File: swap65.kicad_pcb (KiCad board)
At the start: 2 copper layers, 309.6 x 100 mm, 167 parts, among them J1 SWD, J2 USB_C_Receptacle_USB2.0, SW1 SW_Push, SW10 Z, SW11 LWin, SW12 2, SW13 W, SW14 S, SW15 X, SW16 LAlt, SW17 3, SW18 E, SW19 D, SW2 Esc, SW20 C, SW21 4, SW22 R, SW23 F, SW24 V, SW25 5, SW26 T, SW27 G, SW28 B, SW29 Space, SW3 Tab, SW30 6, SW31 Y, SW32 H, SW33 N, SW34 7, SW35 U, SW36 J, SW37 M, SW38 8, SW39 I, SW4 Caps, SW40 K, SW41 Comma, SW42 9, SW43 O, SW44 L, SW45 Period, SW46 RAlt, SW47 0, SW48 P, SW49 Colon, SW5 LShift, SW50 Slash, SW51 Fn, SW52 Minus, SW53 [, SW54 Quote, SW55 Plus, SW56 ], SW57 Enter, SW58 RShift, SW59 Left, SW6 LCtrl, SW60 Pipe, SW61 BkSlsh, SW62 Up, SW63 Down, SW64 BkSpc, SW65 Tilde, SW66 Right, SW7 1, SW8 Q, SW9 A, U1 RP2040, U2 USBLC6-2SC6, U3 XC6206PxxxMR, U4 W25Q128JVS, Y1 12MHz

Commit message: routed columns
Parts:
- removed the J1 at (346.4, 143.6)
- added SW2: SW_Push, Button_Switch_SMD:SW_SPST_SKQG_WithStem, B.Cu at (351.3, 142.3)
- moved R3 8.39 mm to (347.0, 132.5), turned to 0 degrees
- moved C9 0.17 mm to (357.7, 128.8)
- turned S2 to 0 degrees
- renumbered C3 to C2, C4 to C3, C2 to C4, D57 to D56, D58 to D57, D59 to D58, D60 to D59, D56 to D60, J2 to J1, SW9 to SW10, SW10 to SW11, SW11 to SW12, SW12 to SW13, SW13 to SW14, SW14 to SW15, SW15 to SW16, SW16 to SW17, SW17 to SW18, SW18 to SW19, SW19 to SW20, SW20 to SW21, SW21 to SW22, SW22 to SW23, SW23 to SW24, SW24 to SW25, SW25 to SW26, SW26 to SW27, SW27 to SW28, SW28 to SW29, SW2 to SW3, SW29 to SW30, SW30 to SW31, SW31 to SW32, SW32 to SW33, SW33 to SW34, SW34 to SW35, SW35 to SW36, SW36 to SW37, SW37 to SW38, SW38 to SW39, SW3 to SW4, SW39 to SW40, SW40 to SW41, SW41 to SW42, SW42 to SW43, SW43 to SW44, SW44 to SW45, SW45 to SW46, SW46 to SW47, SW47 to SW48, SW48 to SW49, SW4 to SW5, SW49 to SW50, SW50 to SW51, SW51 to SW52, SW52 to SW53, SW53 to SW54, SW54 to SW55, SW55 to SW56, SW56 to SW57, SW5 to SW6, SW57 to SW62, SW62 to SW63, SW63 to SW64, SW64 to SW65, SW65 to SW66, SW66 to SW67, SW6 to SW7, SW7 to SW8, SW8 to SW9
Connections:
- net Net-(C3-Pad2) renamed /XIN
- net Net-(C4-Pad2) renamed /XOUT
- D1 pad 1: ROW1 -> ROW0
- D10 pad 1: ROW5 -> ROW4
- D11 pad 1: ROW1 -> ROW0
- D12 pad 1: ROW2 -> ROW1
- D13 pad 1: ROW3 -> ROW2
- D14 pad 1: ROW4 -> ROW3
- D15 pad 1: ROW5 -> ROW4
- D16 pad 1: ROW1 -> ROW0
- D17 pad 1: ROW2 -> ROW1
- D18 pad 1: ROW3 -> ROW2
- D19 pad 1: ROW4 -> ROW3
- D2 pad 1: ROW2 -> ROW1
- D20 pad 1: ROW1 -> ROW0
- D21 pad 1: ROW2 -> ROW1
- D22 pad 1: ROW3 -> ROW2
- D23 pad 1: ROW4 -> ROW3
- D24 pad 1: ROW1 -> ROW0
- D25 pad 1: ROW2 -> ROW1
- D26 pad 1: ROW3 -> ROW2
- D27 pad 1: ROW4 -> ROW3
- D28 pad 1: ROW5 -> ROW4
- D29 pad 1: ROW1 -> ROW0
- D3 pad 1: ROW3 -> ROW2
- D30 pad 1: ROW2 -> ROW1
- D31 pad 1: ROW3 -> ROW2
- D32 pad 1: ROW4 -> ROW3
- D33 pad 1: ROW1 -> ROW0
- D34 pad 1: ROW2 -> ROW1
- D35 pad 1: ROW3 -> ROW2
- D36 pad 1: ROW4 -> ROW3
- D37 pad 1: ROW1 -> ROW0
- D38 pad 1: ROW2 -> ROW1
- D39 pad 1: ROW3 -> ROW2
- D4 pad 1: ROW4 -> ROW3
- D40 pad 1: ROW4 -> ROW3
- D41 pad 1: ROW1 -> ROW0
- D42 pad 1: ROW2 -> ROW1
- D43 pad 1: ROW3 -> ROW2
- D44 pad 1: ROW4 -> ROW3
- D45 pad 1: ROW5 -> ROW4
- D46 pad 1: ROW1 -> ROW0
- D47 pad 1: ROW2 -> ROW1
- D48 pad 1: ROW3 -> ROW2
- D49 pad 1: ROW4 -> ROW3
- D5 pad 1: ROW5 -> ROW4
- D50 pad 1: ROW5 -> ROW4
- D51 pad 1: ROW1 -> ROW0
- D52 pad 1: ROW2 -> ROW1
- D53 pad 1: ROW3 -> ROW2
- D54 pad 1: ROW1 -> ROW0
- D55 pad 1: ROW2 -> ROW1
- D56 pad 1: ROW4 -> ROW3
- D57 pad 1: ROW5 -> ROW4
- D58 pad 1: ROW1 -> ROW0
- D59 pad 1: ROW2 -> ROW1
- D6 pad 1: ROW1 -> ROW0
- D60 pad 1: ROW3 -> ROW2
- D61 pad 1: ROW4 -> ROW3
- D62 pad 1: ROW5 -> ROW4
- D63 pad 1: ROW1 -> ROW0
- D64 pad 1: ROW5 -> ROW4
- D7 pad 1: ROW2 -> ROW1
- D8 pad 1: ROW3 -> ROW2
- D9 pad 1: ROW4 -> ROW3
- U1 pad 11: unconnected-(U1-Pad11) -> COL6
- U1 pad 12: unconnected-(U1-Pad12) -> COL5
- U1 pad 13: unconnected-(U1-Pad13) -> COL4
- U1 pad 14: unconnected-(U1-Pad14) -> COL3
- U1 pad 15: unconnected-(U1-Pad15) -> COL2
- U1 pad 16: unconnected-(U1-Pad16) -> COL1
- U1 pad 17: unconnected-(U1-Pad17) -> COL0
- U1 pad 2: unconnected-(U1-Pad2) -> COL14
- U1 pad 24: SWCLK -> unconnected-(U1-Pad24)
- U1 pad 25: SWD -> unconnected-(U1-Pad25)
- U1 pad 3: unconnected-(U1-Pad3) -> COL13
- U1 pad 4: unconnected-(U1-Pad4) -> COL12
- U1 pad 5: unconnected-(U1-Pad5) -> COL11
- U1 pad 6: unconnected-(U1-Pad6) -> COL10
- U1 pad 7: unconnected-(U1-Pad7) -> COL9
- U1 pad 8: unconnected-(U1-Pad8) -> COL8
- U1 pad 9: unconnected-(U1-Pad9) -> COL7
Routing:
- net COL0: track 85.1 -> 392.7 mm, vias 0 -> 1
- net ROW5: track 283.9 -> 0.00 mm
- net COL1: track 96.3 -> 376.3 mm, vias 0 -> 1
- net COL2: track 91.0 -> 352.2 mm, vias 0 -> 1
- net ROW0: track 0.00 -> 255.1 mm
- net COL3: track 67.0 -> 306.8 mm, vias 0 -> 1
- net COL4: track 67.0 -> 288.2 mm, vias 0 -> 1
- net COL5: track 87.0 -> 290.2 mm, vias 0 -> 1
- net COL6: track 67.0 -> 251.8 mm, vias 0 -> 1
- net COL7: track 67.0 -> 251.3 mm, vias 0 -> 1
- net COL8: track 67.0 -> 234.9 mm, vias 0 -> 1
- net COL9: track 87.0 -> 229.0 mm, vias 0 -> 1
- net COL11: track 44.0 -> 182.6 mm, vias 0 -> 1
- net COL10: track 87.0 -> 210.9 mm, vias 0 -> 1
- net COL12: track 84.1 -> 183.9 mm, vias 0 -> 1
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
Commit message: completed first pass at routing
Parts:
- SW60, SW65, SW66: footprint marbastlib-mx:SW_MX_HS_1u -> marbastlib-mx:SW_MX_HS_S_1u
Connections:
- U1 pad 29: unconnected-(U1-Pad29) -> ROW4
- U1 pad 30: unconnected-(U1-Pad30) -> ROW3
- U1 pad 31: unconnected-(U1-Pad31) -> ROW2
- U1 pad 35: unconnected-(U1-Pad35) -> ROW1
- U1 pad 36: unconnected-(U1-Pad36) -> ROW0
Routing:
- net ROW4: track 286.4 -> 333.7 mm, vias 0 -> 2
- net ROW3: track 254.8 -> 297.8 mm, vias 0 -> 2
- net ROW0: track 255.1 -> 293.7 mm
- net ROW2: track 247.7 -> 283.6 mm
- net ROW1: track 257.2 -> 271.1 mm
- net Net-(D58-Pad2): track 28.6 -> 27.0 mm
- net COL0: track 392.7 -> 391.2 mm

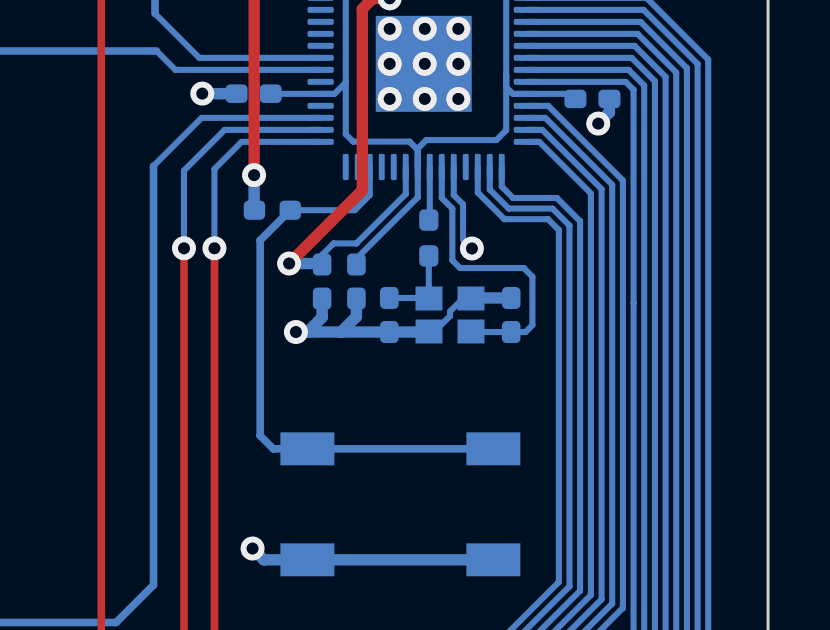
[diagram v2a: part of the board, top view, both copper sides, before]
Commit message: added screen header to schematic
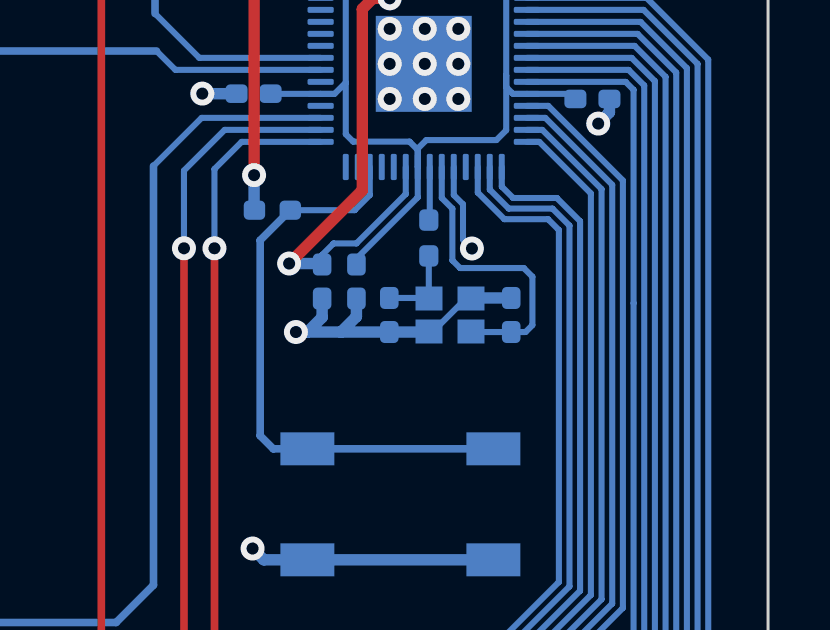
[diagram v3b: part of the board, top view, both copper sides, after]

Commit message: completed route pass 1
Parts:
- added J2: OLED, Connector_PinHeader_2.54mm:PinHeader_1x04_P2.54mm_Vertical, F.Cu at (350.5, 154.9)
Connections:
- U1 pad 38: unconnected-(U1-Pad38) -> SCL
- U1 pad 39: unconnected-(U1-Pad39) -> SDA

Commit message: routed usb and jst connector
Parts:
- removed the R5 at (346.2, 99.4)
- added J3: DB, Connector_JST:JST_SH_SM04B-SRSS-TB_1x04-1MP_P1.00mm_Horizontal, B.Cu at (352.7, 117.9)
- U2: value USBLC6-2SC6 -> SRV05-4; footprint Package_TO_SOT_SMD:SOT-23-6 -> marbastlib-various:SOT-23-6-routable
- moved J2 36.2 mm to (345.2, 119.1)
- moved C1 21.4 mm to (365.8, 120.7), turned to 180 degrees
- moved C10 19.3 mm to (348.2, 138.7), turned to 180 degrees
- moved C16 18.7 mm to (359.9, 136.2), turned to 0 degrees
- moved C11 17.3 mm to (358.1, 130.8), turned to 0 degrees
- moved R3 16.6 mm to (352.9, 148.1), turned to -90 degrees
- moved C15 16.3 mm to (355.9, 140.7), turned to -90 degrees
- moved R1 12.9 mm to (357.6, 128.8)
- moved R2 12.9 mm to (356.1, 128.8)
- moved SW1 11.9 mm to (371.0, 104.3)
- moved R5 11.9 mm to (367.0, 108.0)
- moved C6 11.7 mm to (358.1, 131.9)
- moved SW2 11.6 mm to (351.0, 153.9), turned to -90 degrees
- moved C2 10.2 mm to (349.1, 144.3), turned to 180 degrees
- moved U3 10.1 mm to (368.3, 115.2)
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- renumbered C17 to C1, C7 to C10, C8 to C11, C9 to C12, C10 to C13, C11 to C14, C12 to C15, C13 to C16, C14 to C17, C15 to C4, C16 to C5, C1 to C6, C4 to C7, C5 to C8, C6 to C9, R8 to R5, U4 to U3, U3 to U4
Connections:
- J1 pad A6: D_USB_P -> D_P
- J1 pad A7: D_USB_N -> D_N
- J1 pad B6: D_USB_P -> D_P
- J1 pad B7: D_USB_N -> D_N
- J1 pad S1: Net-(J1-PadS1) -> GND
- U2 pad 1: D_P -> unconnected-(U2-Pad1)
- U2 pad 3: D_N -> D_P
- U2 pad 4: D_USB_N -> D_N
- U2 pad 5: +5V -> VBUS
- U2 pad 6: D_USB_P -> unconnected-(U2-Pad6)
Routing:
- net COL0: track 391.2 -> 0.00 mm, vias 1 -> 0
- net COL1: track 376.3 -> 0.00 mm, vias 1 -> 0
- net COL2: track 352.2 -> 0.00 mm, vias 1 -> 0
- net ROW4: track 333.7 -> 0.00 mm, vias 2 -> 0
- net COL3: track 306.8 -> 0.00 mm, vias 1 -> 0
- net ROW3: track 297.8 -> 0.00 mm, vias 2 -> 0
- net ROW0: track 293.7 -> 0.00 mm
- net COL5: track 290.2 -> 0.00 mm, vias 1 -> 0
- net COL4: track 288.2 -> 0.00 mm, vias 1 -> 0
- net ROW2: track 283.6 -> 0.00 mm
- net ROW1: track 271.1 -> 0.00 mm
- net COL6: track 251.8 -> 0.00 mm, vias 1 -> 0
- net COL7: track 251.3 -> 0.00 mm, vias 1 -> 0
- net COL8: track 234.9 -> 0.00 mm, vias 1 -> 0
- net COL9: track 229.0 -> 0.00 mm, vias 1 -> 0
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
